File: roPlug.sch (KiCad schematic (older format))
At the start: 18 parts, among them P1 USB_C_Plug, SW1 Rotary_Encoder_Switch, U1 ATmega32U4-MU, Y1 16MHz

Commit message: change edgemount usb plug to sidemount due to supply issues with pcba
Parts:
- P1: footprint misc:GCT_USB4155-03-C_REVA -> Connector_USB:USB_C_Plug_Molex_105444
- RST1: footprint Connector_PinHeader_2.54mm:PinHeader_1x01_P2.54mm_Vertical -> Connector_PinSocket_2.54mm:PinSocket_1x01_P2.54mm_Vertical
- Y1: footprint Crystal:Crystal_SMD_0603-4Pin_6.0x3.5mm -> Crystal:Crystal_SMD_Abracon_ABM3B-4Pin_5.0x3.2mm
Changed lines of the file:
@@
 F 0 "Y1" V 2104 2794 50  0000 L CNN
 F 1 "16MHz" V 2195 2794 50  0000 L CNN
-F 2 "Crystal:Crystal_SMD_0603-4Pin_6.0x3.5mm" H 2150 2650 50  0001 C CNN
+F 2 "Crystal:Crystal_SMD_Abracon_ABM3B-4Pin_5.0x3.2mm" H 2150 2650 50  0001 C CNN
 F 3 "~" H 2150 2650 50  0001 C CNN
 	1    2150 2650
@@
 F 0 "P1" H 7957 4067 50  0000 C CNN
 F 1 "USB_C_Plug" H 7957 3976 50  0000 C CNN
-F 2 "misc:GCT_USB4155-03-C_REVA" H 8000 2800 50  0001 C CNN
+F 2 "Connector_USB:USB_C_Plug_Molex_105444" H 8000 2800 50  0001 C CNN
 F 3 "https://www.usb.org/sites/default/files/documents/usb_type-c.zip" H 8000 2800 50  0001 C CNN
 	1    7850 2800
@@
 F 0 "RST1" H 2342 2125 50  0000 C CNN
 F 1 "Conn_01x01_Female" H 2342 2216 50  0000 C CNN
-F 2 "Connector_PinHeader_2.54mm:PinHeader_1x01_P2.54mm_Vertical" H 2450 2350 50  0001 C CNN
+F 2 "Connector_PinSocket_2.54mm:PinSocket_1x01_P2.54mm_Vertical" H 2450 2350 50  0001 C CNN
 F 3 "~" H 2450 2350 50  0001 C CNN
 	1    2450 2350

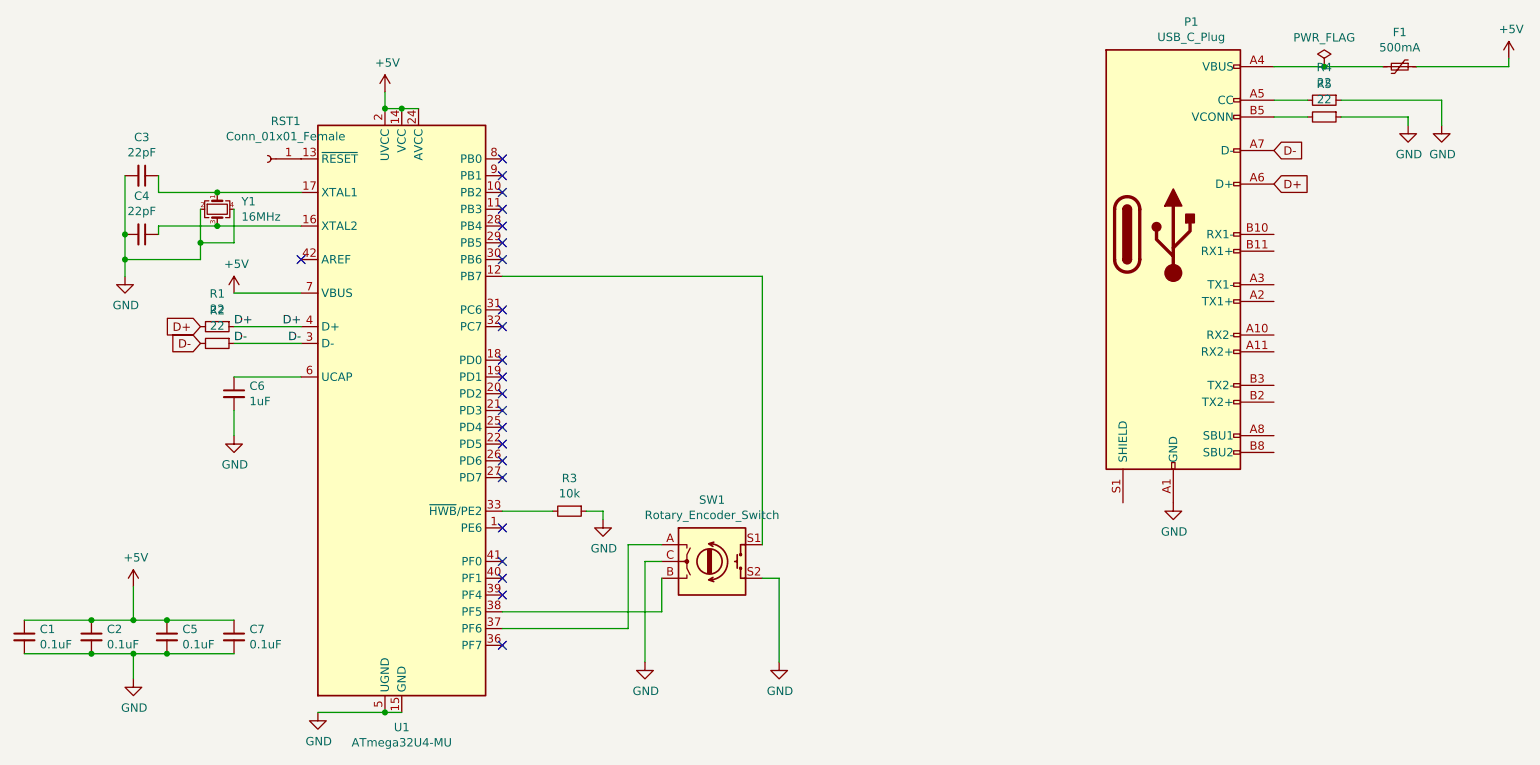
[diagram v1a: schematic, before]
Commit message: update schematics and fix USB-C circuitry for host detection
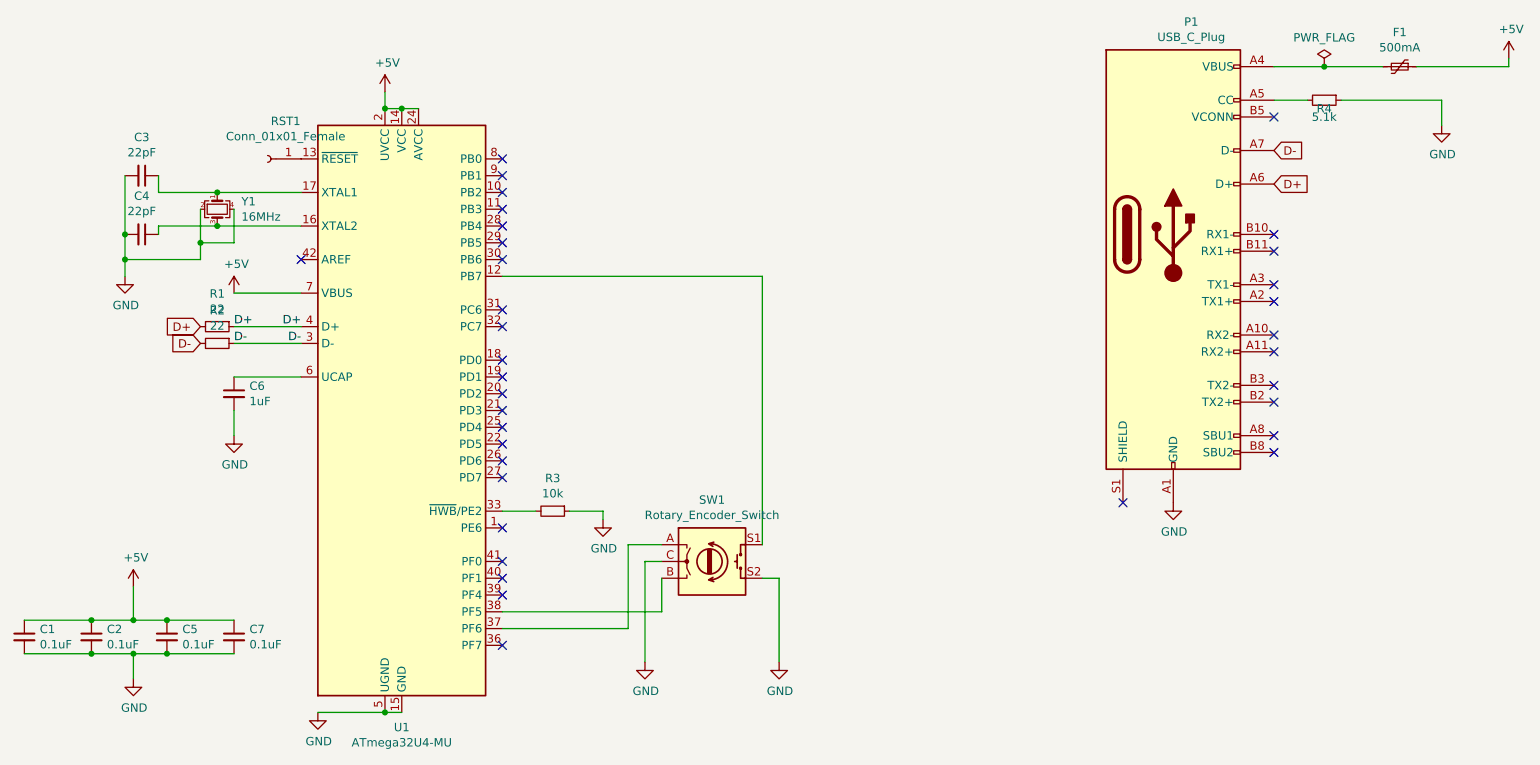
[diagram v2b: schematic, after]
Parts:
- removed R5: 22, Resistor_SMD:R_0603_1608Metric, symbol Device:R_Small
- R4: value 22 -> 5.1k
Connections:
- no-connect marks 23 -> 35
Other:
- moved on the sheet: R3
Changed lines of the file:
@@
 L Device:R_Small R3
 U 1 1 615C1DAA
-P 4250 4450
-F 0 "R3" V 4054 4450 50  0000 C CNN
-F 1 "10k" V 4145 4450 50  0000 C CNN
-F 2 "Resistor_SMD:R_0603_1608Metric" H 4250 4450 50  0001 C CNN
-F 3 "~" H 4250 4450 50  0001 C CNN
-	1    4250 4450
+P 4150 4450
+F 0 "R3" V 3954 4450 50  0000 C CNN
+F 1 "10k" V 4045 4450 50  0000 C CNN
+F 2 "Resistor_SMD:R_0603_1608Metric" H 4150 4450 50  0001 C CNN
+F 3 "~" H 4150 4450 50  0001 C CNN
+	1    4150 4450
 	0    1    1    0
 $EndComp
@@
 	2750 5650 3150 5650
 Wire Wire Line
-	4350 4450 4450 4450
-Wire Wire Line
-	3850 4450 4150 4450
+	4250 4450 4450 4450
+Wire Wire Line
+	3850 4450 4050 4450
 Wire Wire Line
 	2650 2550 2150 2550
@@
 Wire Wire Line
 	9850 1800 9850 1750
-Wire Wire Line
-	9300 1800 9850 1800
 $Comp
 L power:+5V #PWR014
@@
 $EndComp
 Connection ~ 8750 1800
-Wire Wire Line
-	8750 1800 9100 1800
 $Comp
 L power:GND #PWR011
@@
 U 1 1 6165C701
 P 8750 2000
-F 0 "R4" V 8554 2000 50  0000 C CNN
-F 1 "22" V 8645 2000 50  0000 C CNN
+F 0 "R4" V 8800 2000 50  0000 C CNN
+F 1 "5.1k" V 8850 2000 50  0000 C CNN
 F 2 "Resistor_SMD:R_0603_1608Metric" H 8750 2000 50  0001 C CNN
 F 3 "~" H 8750 2000 50  0001 C CNN
@@
 	0    1    1    0
 $EndComp
-$Comp
-L Device:R_Small R5
-U 1 1 6165E361
-P 8750 2100
-F 0 "R5" V 8554 2100 50  0000 C CNN
-F 1 "22" V 8645 2100 50  0000 C CNN
-F 2 "Resistor_SMD:R_0603_1608Metric" H 8750 2100 50  0001 C CNN
-F 3 "~" H 8750 2100 50  0001 C CNN
-	1    8750 2100
-	0    1    1    0
-$EndComp
-$Comp
-L power:GND #PWR012
-U 1 1 6165F6F1
-P 9250 2150
-F 0 "#PWR012" H 9250 1900 50  0001 C CNN
-F 1 "GND" H 9255 1977 50  0000 C CNN
-F 2 "" H 9250 2150 50  0001 C CNN
-F 3 "" H 9250 2150 50  0001 C CNN
-	1    9250 2150
-	1    0    0    -1
-$EndComp
-$Comp
-L power:GND #PWR013
-U 1 1 6165FE1F
-P 9450 2150
-F 0 "#PWR013" H 9450 1900 50  0001 C CNN
-F 1 "GND" H 9455 1977 50  0000 C CNN
-F 2 "" H 9450 2150 50  0001 C CNN
-F 3 "" H 9450 2150 50  0001 C CNN
-	1    9450 2150
-	1    0    0    -1
-$EndComp
 Wire Wire Line
 	8450 2000 8650 2000
-Wire Wire Line
-	9450 2000 9450 2150
-Wire Wire Line
-	8850 2000 9450 2000
-Wire Wire Line
-	9250 2150 9250 2100
-Wire Wire Line
-	9250 2100 8850 2100
-Wire Wire Line
-	8650 2100 8450 2100
 $Comp
 L Device:Rotary_Encoder_Switch SW1
@@
 	-1   0    0    1
 $EndComp
+Wire Wire Line
+	8750 1800 9100 1800
+Wire Wire Line
+	8850 2000 9450 2000
+$Comp
+L power:GND #PWR013
+U 1 1 6165FE1F
+P 9450 2150
+F 0 "#PWR013" H 9450 1900 50  0001 C CNN
+F 1 "GND" H 9455 1977 50  0000 C CNN
+F 2 "" H 9450 2150 50  0001 C CNN
+F 3 "" H 9450 2150 50  0001 C CNN
+	1    9450 2150
+	1    0    0    -1
+$EndComp
+Wire Wire Line
+	9300 1800 9850 1800
+Wire Wire Line
+	9450 2000 9450 2150
+NoConn ~ 8450 2100
+NoConn ~ 8450 2800
+NoConn ~ 8450 2900
+NoConn ~ 7550 4400
+NoConn ~ 8450 4100
+NoConn ~ 8450 4000
+NoConn ~ 8450 3800
+NoConn ~ 8450 3700
+NoConn ~ 8450 3500
+NoConn ~ 8450 3400
+NoConn ~ 8450 3200
+NoConn ~ 8450 3100
 $EndSCHEMATC
